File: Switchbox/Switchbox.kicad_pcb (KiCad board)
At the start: 2 copper layers, 90 x 68 mm, 37 parts, among them J1 USB-C_connector, SW1 SW_SPDT, SW2 SW_SPDT, SW3 SW_SPDT, SW4 SW_SPDT, SW5 SW_SPST_LED, SW6 SW_SPDT_BOX, U2 AP63203WU

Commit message: NO ERRORSgit add *git add *git add *git add * YAY
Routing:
- net GND: track 212.9 -> 37.2 mm, vias 3 -> 10
- net BOX_STATE: track 98.5 -> 97.4 mm

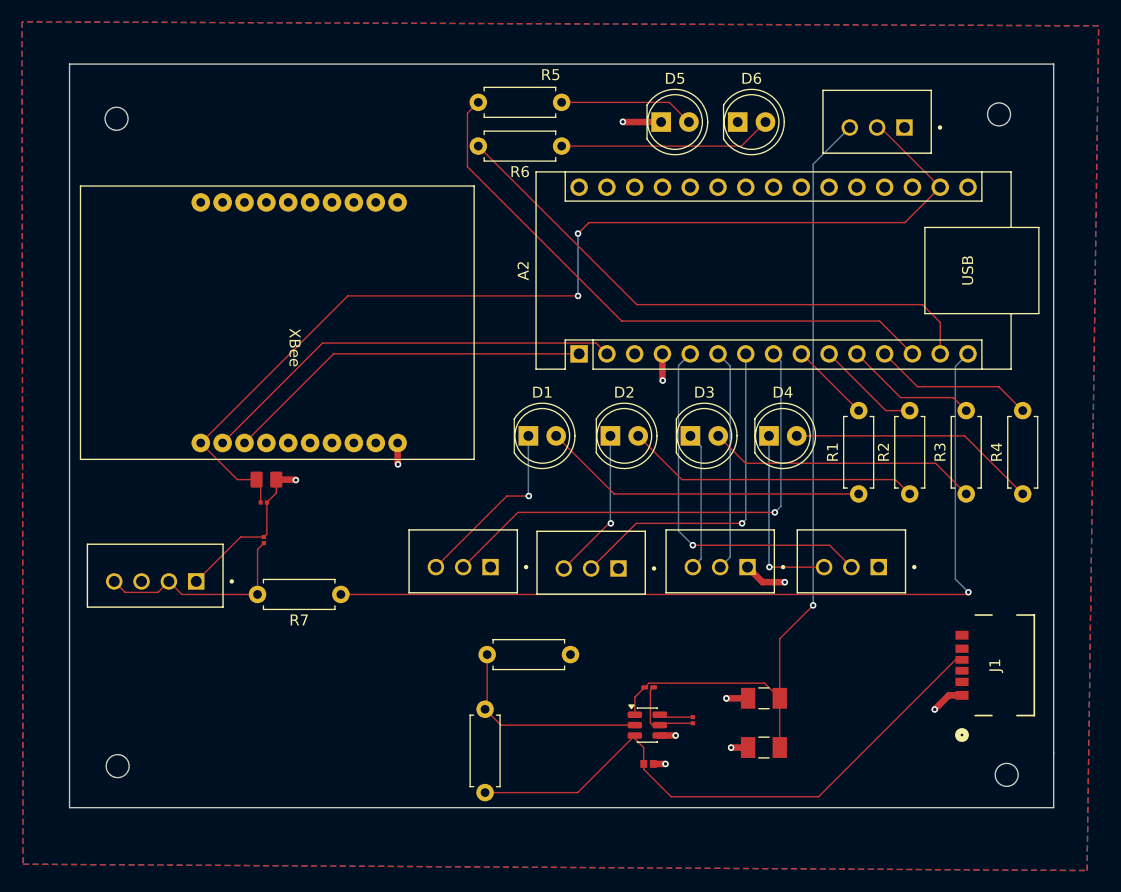
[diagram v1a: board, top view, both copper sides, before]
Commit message: added rounded edges
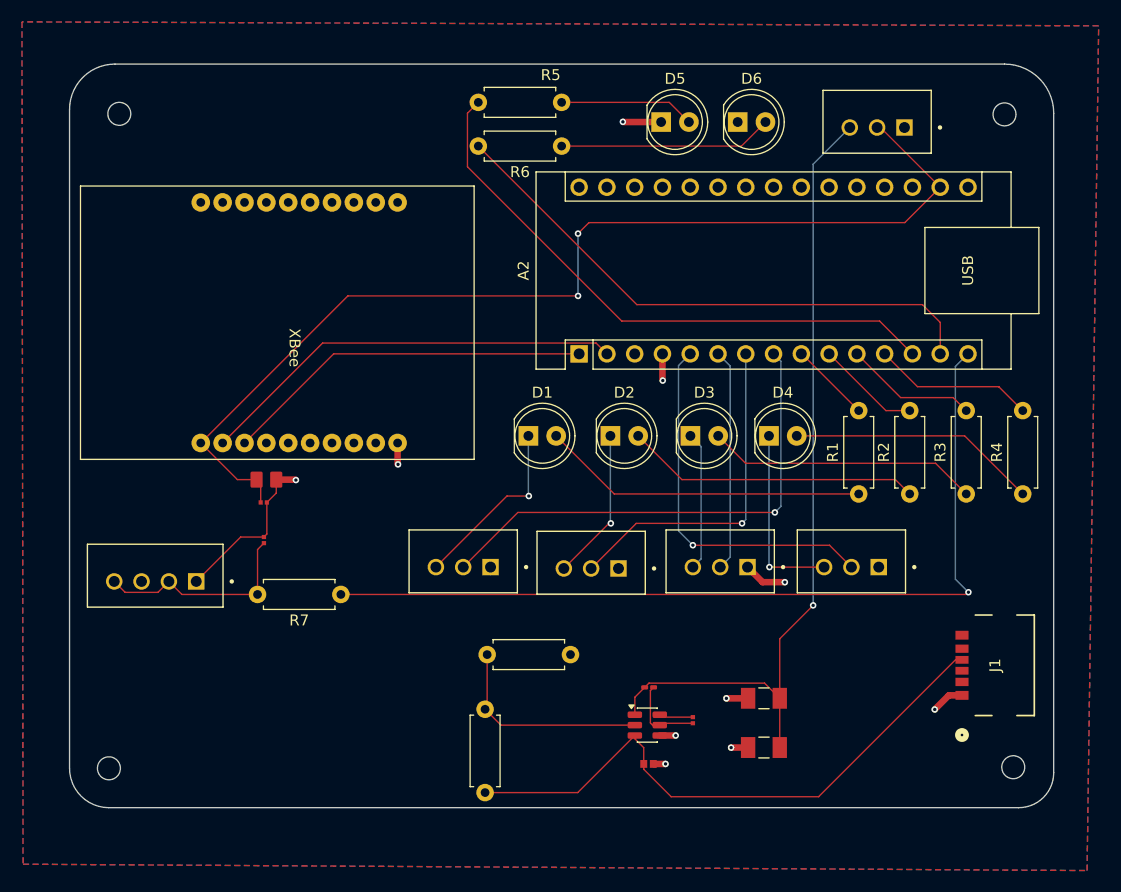
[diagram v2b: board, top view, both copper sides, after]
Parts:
- moved REF** 0.92 mm to (189.3, 149.3)
- moved REF** 0.82 mm to (106.6, 149.4)
- moved REF** 0.51 mm to (107.5, 89.5)
- moved REF** 0.50 mm to (188.5, 89.6)
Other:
- outline, holes or cut-outs redrawn
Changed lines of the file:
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@@
 	(footprint "MountingHole:MountingHole_2.1mm"
 		(layer "F.Cu")
-		(at 188.7 150)
+		(at 189.3 149.3)
 		(descr "Mounting Hole 2.1mm, no annular, generated by kicad-footprint-generator mountinghole.py")
 		(tags "mountinghole")
@@
 	(footprint "MountingHole:MountingHole_2.1mm"
 		(layer "F.Cu")
-		(at 107.3 90)
+		(at 107.55 89.55)
 		(descr "Mounting Hole 2.1mm, no annular, generated by kicad-footprint-generator mountinghole.py")
 		(tags "mountinghole")
@@
 	(footprint "MountingHole:MountingHole_2.1mm"
 		(layer "F.Cu")
-		(at 188 89.6)
+		(at 188.5 89.6)
 		(descr "Mounting Hole 2.1mm, no annular, generated by kicad-footprint-generator mountinghole.py")
 		(tags "mountinghole")
@@
 	(footprint "MountingHole:MountingHole_2.1mm"
 		(layer "F.Cu")
-		(at 107.4 149.2)
+		(at 106.6 149.4)
 		(descr "Mounting Hole 2.1mm, no annular, generated by kicad-footprint-generator mountinghole.py")
 		(tags "mountinghole")
@@
 		)
 	)
-	(gr_line
-		(start 193 85)
-		(end 193 148)
+	(gr_arc
+		(start 103 89.15)
+		(mid 104.215507 86.215507)
+		(end 107.15 85)
 		(stroke
 			(width 0.0381)
@@
 	)
 	(gr_line
-		(start 193 153)
-		(end 193 148)
+		(start 107.15 85)
+		(end 188.5 85)
+		(stroke
+			(width 0.0381)
+			(type default)
+		)
+		(layer "Edge.Cuts")
+	)
+	(gr_arc
+		(start 106.6 153)
+		(mid 104.054416 151.945584)
+		(end 103 149.4)
+		(stroke
+			(width 0.0381)
+			(type default)
+		)
+		(layer "Edge.Cuts")
+	)
+	(gr_arc
+		(start 193 149.8)
+		(mid 192.062742 152.062742)
+		(end 189.8 153)
+		(stroke
+			(width 0.0381)
+			(type default)
+		)
+		(layer "Edge.Cuts")
+	)
+	(gr_arc
+		(start 188.5 85)
+		(mid 191.681981 86.318019)
+		(end 193 89.5)
 		(stroke
 			(width 0.0381)
@@
 	)
 	(gr_line
-		(start 193 85)
-		(end 103 85)
+		(start 193 89.5)
+		(end 193 149.8)
 		(stroke
 			(width 0.0381)
@@
 	)
 	(gr_line
-		(start 103 153)
-		(end 193 153)
+		(start 103 89.15)
+		(end 103 149.4)
 		(stroke
 			(width 0.0381)
@@
 	)
 	(gr_line
-		(start 103 85)
-		(end 103 153)
+		(start 106.6 153)
+		(end 189.8 153)
 		(stroke
 			(width 0.0381)
@@
 		(min_thickness 0.25)
 		(filled_areas_thickness no)
-		(fill yes
+		(fill
 			(thermal_gap 0.5)
 			(thermal_bridge_width 0.5)

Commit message: added some silkscreen text
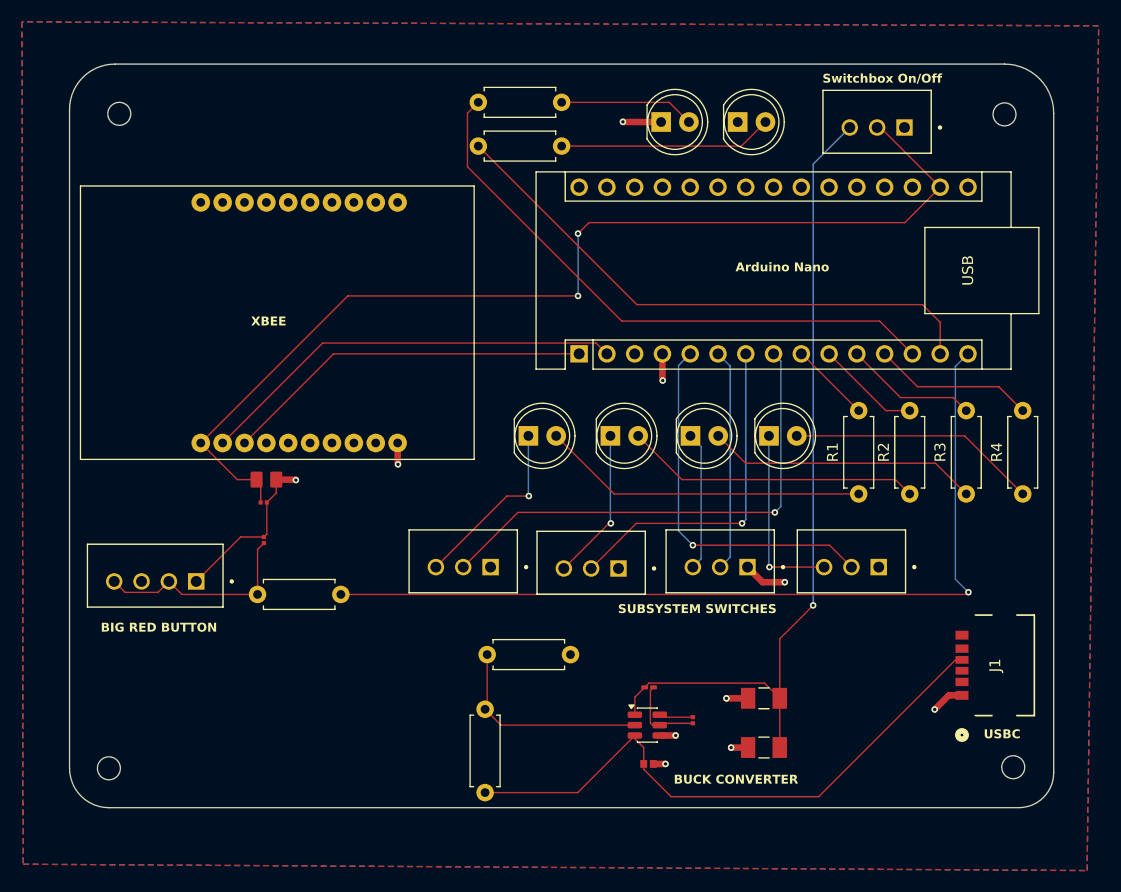
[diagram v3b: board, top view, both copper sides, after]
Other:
- board text added: "Arduino Nano"
- board text added: "BIG RED BUTTON"
- board text added: "BUCK CONVERTER"
- board text added: "SUBSYSTEM SWITCHES"
- board text added: "Switchbox On/Off"
- board text added: "USBC"
- board text added: "XBEE"
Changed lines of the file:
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@@
 			(at 1.27 -3.96 0)
 			(layer "F.SilkS")
+			(hide yes)
 			(effects
 				(font
@@
 			(at 1.27 -3.96 0)
 			(layer "F.SilkS")
+			(hide yes)
 			(effects
 				(font
@@
 			(at 1.27 -3.96 0)
 			(layer "F.SilkS")
+			(hide yes)
 			(effects
 				(font
@@
 			(at 3.81 -2.37 0)
 			(layer "F.SilkS")
+			(hide yes)
 			(effects
 				(font
@@
 			(at 1.27 -3.96 0)
 			(layer "F.SilkS")
+			(hide yes)
 			(effects
 				(font
@@
 			(at 1.27 -3.96 0)
 			(layer "F.SilkS")
+			(hide yes)
 			(effects
 				(font
@@
 			(at 1 2.5 0)
 			(layer "F.SilkS")
+			(hide yes)
 			(effects
 				(font
@@
 		)
 		(property "Value" "680"
-			(at 3.81 2.37 0)
+			(at 3.81 1.37 0)
 			(layer "F.Fab")
 			(effects
@@
 			(at 3.81 -2.37 0)
 			(layer "F.SilkS")
+			(hide yes)
 			(effects
 				(font
@@
 			(layer "F.SilkS")
 		)
-		(fp_text user "XBee"
-			(at -1 2 270)
-			(unlocked yes)
-			(layer "F.SilkS")
-			(effects
-				(font
-					(size 1 1)
-					(thickness 0.1)
-				)
-				(justify left bottom)
-			)
-		)
-		(fp_text user "${REFERENCE}"
-			(at 2 -3 270)
-			(unlocked yes)
-			(layer "F.Fab")
-			(effects
-				(font
-					(size 1 1)
-					(thickness 0.15)
-				)
-			)
-		)
 		(pad "1" thru_hole circle
 			(at -11.5 -6 90)
@@
 			(at 7.62 -5.08 90)
 			(layer "F.SilkS")
+			(hide yes)
 			(effects
 				(font
@@
 			(at 8.89 19.05 0)
 			(layer "F.Fab")
+			(hide yes)
 			(effects
 				(font
@@
 			(at 1.27 -3.96 0)
 			(layer "F.SilkS")
+			(hide yes)
 			(effects
 				(font
@@
 		(layer "Edge.Cuts")
 	)
+	(gr_text "BIG RED BUTTON\n"
+		(at 105.85 137 0)
+		(layer "F.SilkS")
+		(effects
+			(font
+				(size 0.8128 0.8128)
+				(thickness 0.1524)
+				(bold yes)
+			)
+			(justify left bottom)
+		)
+	)
+	(gr_text "SUBSYSTEM SWITCHES\n"
+		(at 153.15 135.3 0)
+		(layer "F.SilkS")
+		(effects
+			(font
+				(size 0.8128 0.8128)
+				(thickness 0.1524)
+				(bold yes)
+			)
+			(justify left bottom)
+		)
+	)
+	(gr_text "USBC"
+		(at 186.590501 146.75 0)
+		(layer "F.SilkS")
+		(effects
+			(font
+				(size 0.8128 0.8128)
+				(thickness 0.1524)
+				(bold yes)
+			)
+			(justify left bottom)
+		)
+	)
+	(gr_text "XBEE"
+		(at 119.6 109 0)
+		(layer "F.SilkS")
+		(effects
+			(font
+				(size 0.8128 0.8128)
+				(thickness 0.1524)
+				(bold yes)
+			)
+			(justify left bottom)
+		)
+	)
+	(gr_text "Switchbox On/Off"
+		(at 171.85 86.8 0)
+		(layer "F.SilkS")
+		(effects
+			(font
+				(size 0.8128 0.8128)
+				(thickness 0.1524)
+				(bold yes)
+			)
+			(justify left bottom)
+		)
+	)
+	(gr_text "BUCK CONVERTER"
+		(at 158.25 150.9 0)
+		(layer "F.SilkS")
+		(effects
+			(font
+				(size 0.8128 0.8128)
+				(thickness 0.1524)
+				(bold yes)
+			)
+			(justify left bottom)
+		)
+	)
+	(gr_text "Arduino Nano\n"
+		(at 163.9 104.05 0)
+		(layer "F.SilkS")
+		(effects
+			(font
+				(size 0.8128 0.8128)
+				(thickness 0.1524)
+				(bold yes)
+			)
+			(justify left bottom)
+		)
+	)
 	(segment

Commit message: added names
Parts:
- added G***: LOGO, LOGO, F.Cu at (116.0, 90.4)
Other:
- board text added: "Switchbox PCB SP26 Fiona Lin Nicole Zhou"
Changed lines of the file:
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@@
 		(embedded_fonts no)
 	)
+	(footprint "LOGO"
+		(layer "F.Cu")
+		(at 115.981386 90.418049)
+		(property "Reference" "G***"
+			(at 0 0 0)
+			(layer "F.SilkS")
+			(hide yes)
+			(effects
+				(font
+					(size 1.5 1.5)
+					(thickness 0.3)
+				)
+			)
+		)
+		(property "Value" "LOGO"
+			(at 0.75 0 0)
+			(layer "F.SilkS")
+			(hide yes)
+			(effects
+				(font
+					(size 1.5 1.5)
+					(thickness 0.3)
+				)
+			)
+		)
+		(property "Datasheet" ""
+			(at 0 0 0)
+			(layer "F.Fab")
+			(hide yes)
+			(effects
+				(font
+					(size 1.27 1.27)
+					(thickness 0.15)
+				)
+			)
+		)
+		(property "Description" ""
+			(at 0 0 0)
+			(layer "F.Fab")
+			(hide yes)
+			(effects
+				(font
+					(size 1.27 1.27)
+					(thickness 0.15)
+				)
+			)
+		)
+		(attr board_only exclude_from_pos_files exclude_from_bom)
+		(fp_poly
+			(pts
+				(xy -1.172331 -0.877812) (xy -1.142119 -0.829444) (xy -1.094422 -0.734718) (xy -0.997407 -0.4798)
+				(xy -0.951237 -0.224085) (xy -0.953033 -0.021328) (xy -0.967611 0.114895) (xy -0.984924 0.204809)
+				(xy -1.01576 0.260418) (xy -1.070903 0.293723) (xy -1.161139 0.316728) (xy -1.275484 0.337507) (xy -1.400253 0.360495)
+				(xy -1.507028 0.381286) (xy -1.579596 0.396672) (xy -1.597197 0.401104) (xy -1.62052 0.40034) (xy -1.616741 0.371381)
+				(xy -1.583482 0.305918) (xy -1.556691 0.259673) (xy -1.402266 -0.055653) (xy -1.284167 -0.417133)
+				(xy -1.202358 -0.824875) (xy -1.198218 -0.853535) (xy -1.189315 -0.883878)
+			)
+			(stroke
+				(width 0)
+				(type solid)
+			)
+			(fill yes)
+			(layer "F.SilkS")
+		)
+		(fp_poly
+			(pts
+				(xy -0.173183 -1.747455) (xy -0.132772 -1.724706) (xy 0.015561 -1.59468) (xy 0.135495 -1.423325)
+				(xy 0.218865 -1.224587) (xy 0.252379 -1.066816) (xy 0.267 -0.975343) (xy 0.284705 -0.931595) (xy 0.310875 -0.924474)
+				(xy 0.320007 -0.92736) (xy 0.441248 -0.966634) (xy 0.600379 -1.007697) (xy 0.77678 -1.045908) (xy 0.949829 -1.076625)
+				(xy 1.036837 -1.088731) (xy 1.261513 -1.103191) (xy 1.466921 -1.091637) (xy 1.63974 -1.055394) (xy 1.726672 -1.020073)
+				(xy 1.836685 -0.942206) (xy 1.9343 -0.837795) (xy 1.998318 -0.729649) (xy 1.999518 -0.726532) (xy 2.022694 -0.620151)
+				(xy 2.031064 -0.478621) (xy 2.025376 -0.323566) (xy 2.00638 -0.17661) (xy 1.976529 -0.06377) (xy 1.860131 0.166044)
+				(xy 1.688955 0.392121) (xy 1.467083 0.611425) (xy 1.198596 0.820922) (xy 0.887578 1.017575) (xy 0.538109 1.19835)
+				(xy 0.154273 1.360212) (xy -0.025935 1.425166) (xy -0.41761 1.545692) (xy -0.786258 1.631775) (xy -1.126275 1.682566)
+				(xy -1.432057 1.697211) (xy -1.683988 1.677145) (xy -1.809565 1.653655) (xy -1.938512 1.624003)
+				(xy -1.993026 1.609223) (xy -2.133836 1.567875) (xy -1.883662 1.54756) (xy -1.710786 1.530333) (xy -1.54897 1.50839)
+				(xy -1.411173 1.483934) (xy -1.310356 1.459166) (xy -1.269492 1.443244) (xy -1.271162 1.420023)
+				(xy -1.327797 1.378278) (xy -1.439737 1.317766) (xy -1.460801 1.30731) (xy -1.631255 1.210542) (xy -1.787878 1.091015)
+				(xy -1.905736 0.980723) (xy -1.99487 0.889714) (xy -2.065734 0.813196) (xy -2.109442 0.761017) (xy -2.11912 0.744307)
+				(xy -2.091301 0.734873) (xy -2.012104 0.715436) (xy -1.887923 0.687295) (xy -1.725149 0.651751)
+				(xy -1.530173 0.610103) (xy -1.309389 0.563651) (xy -1.069188 0.513694) (xy -0.815961 0.461533)
+				(xy -0.556102 0.408468) (xy -0.296002 0.355797) (xy -0.042052 0.304821) (xy 0.199354 0.256839) (xy 0.421825 0.213151)
+				(xy 0.618969 0.175058) (xy 0.784394 0.143859) (xy 0.911708 0.120853) (xy 0.994519 0.10734) (xy 1.026434 0.10462)
+				(xy 1.026496 0.104671) (xy 1.01485 0.130722) (xy 0.973624 0.188576) (xy 0.913385 0.263711) (xy 0.84509 0.351195)
+				(xy 0.819527 0.398651) (xy 0.836193 0.405447) (xy 0.894587 0.370956) (xy 0.959858 0.322038) (xy 1.122123 0.163919)
+				(xy 1.246783 -0.020723) (xy 1.325384 -0.217997) (xy 1.343647 -0.308444) (xy 1.347004 -0.425172)
+				(xy 1.318048 -0.51439) (xy 1.252216 -0.578419) (xy 1.144945 -0.619577) (xy 0.991668 -0.640184) (xy 0.787824 -0.642561)
+				(xy 0.693209 -0.639027) (xy 0.550855 -0.630965) (xy 0.427299 -0.62158) (xy 0.335996 -0.612051) (xy 0.290887 -0.603753)
+				(xy 0.25685 -0.565477) (xy 0.219581 -0.483452) (xy 0.193057 -0.399729) (xy 0.135075 -0.213385) (xy 0.073176 -0.064419)
+				(xy 0.010673 0.040726) (xy -0.04912 0.095604) (xy -0.064397 0.100973) (xy -0.220531 0.133542) (xy -0.376512 0.164004)
+				(xy -0.521443 0.190467) (xy -0.644429 0.211042) (xy -0.734572 0.22384) (xy -0.780977 0.226969) (xy -0.784613 0.225892)
+				(xy -0.783892 0.192425) (xy -0.76647 0.122334) (xy -0.749257 0.069012) (xy -0.71617 -0.065419) (xy -0.693578 -0.236305)
+				(xy -0.682662 -0.421977) (xy -0.6846 -0.600769) (xy -0.700575 -0.751011) (xy -0.70371 -0.767151)
+				(xy -0.746382 -0.916427) (xy -0.812505 -1.08457) (xy -0.891376 -1.247642) (xy -0.972295 -1.381704)
+				(xy -0.988161 -1.403425) (xy -1.042652 -1.484077) (xy -1.051526 -1.531717) (xy -1.011228 -1.554514)
+				(xy -0.919757 -1.560628) (xy -0.675715 -1.587166) (xy -0.429416 -1.666195) (xy -0.362729 -1.696076)
+				(xy -0.271889 -1.736952) (xy -0.214891 -1.753308)
+			)
+			(stroke
+				(width 0)
+				(type solid)
+			)
+			(fill yes)
+			(layer "F.SilkS")
+		)
+		(embedded_fonts no)
+	)
 	(footprint "switchbox_footprints:4_pin_header"
 		(layer "F.Cu")
@@
 				(bold yes)
 			)
+			(justify left bottom)
+		)
+	)
+	(gr_text "Switchbox PCB\nSP26\nFiona Lin\nNicole Zhou"
+		(at 119 93 0)
+		(layer "F.SilkS")
+		(effects
+			(font
+				(size 0.9 0.9)
+				(thickness 0.14)
+				(bold yes)
+			)

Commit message: added fish
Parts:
- added G***: LOGO, LOGO, F.Cu at (178.6, 138.5)
- added G***: LOGO, LOGO, F.Cu at (180.9, 149.3)
- added G***: LOGO, LOGO, F.Cu at (173.7, 143.0)

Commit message: I'D LIKE TO BE UNDER THE SEA IN AN OCTOPUS'S GARDEN IN THE SHAAAAAADE
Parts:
- added G***: LOGO, LOGO, F.Cu at (127.5, 143.5)
